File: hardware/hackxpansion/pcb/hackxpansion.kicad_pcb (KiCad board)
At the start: 4 copper layers, 52 x 65 mm, 101 parts, among them CN1 533981471, CN2 533981471, CN3 533981471, CN4 533981471, IC1 ADS7128IRTET, J1 Conn_01x03_MountingPin, J2 USB_C_Receptacle_USB2.0_14P, Q1 BSS138, Q2 2N7002, SW1 SW_Push, SW2 SW_Push, SW3 SW_On_Off, U2 RP2354B, U5 SPX3819M5-L-3-3, U7 BQ24075RGT, U8 USBLC6-2SC6, Y1 ABM8-272-T3

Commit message: updated part numbers
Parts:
- R22: value 3k9 -> 3k3
- R26, R27, R28, R29: value 5R -> 5R1

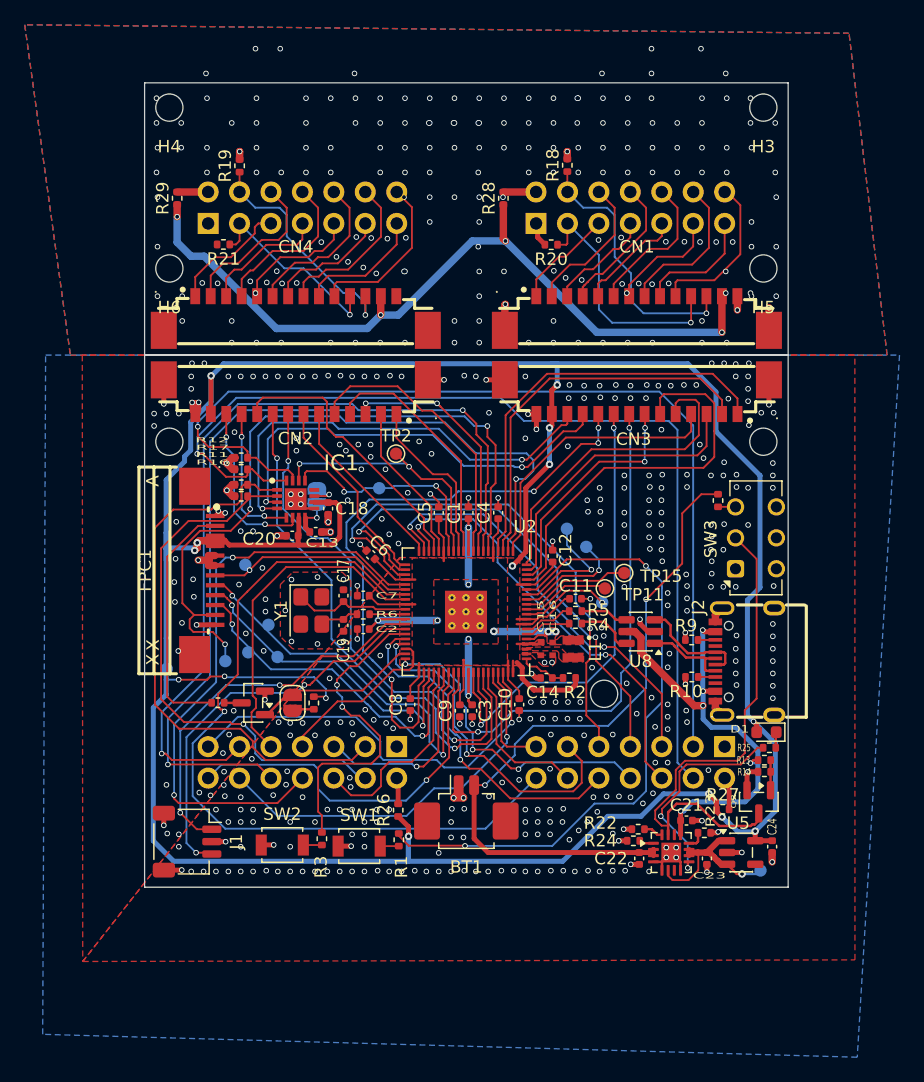
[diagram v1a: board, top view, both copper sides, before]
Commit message: added a bunch of gnd return VIAs, removed via group
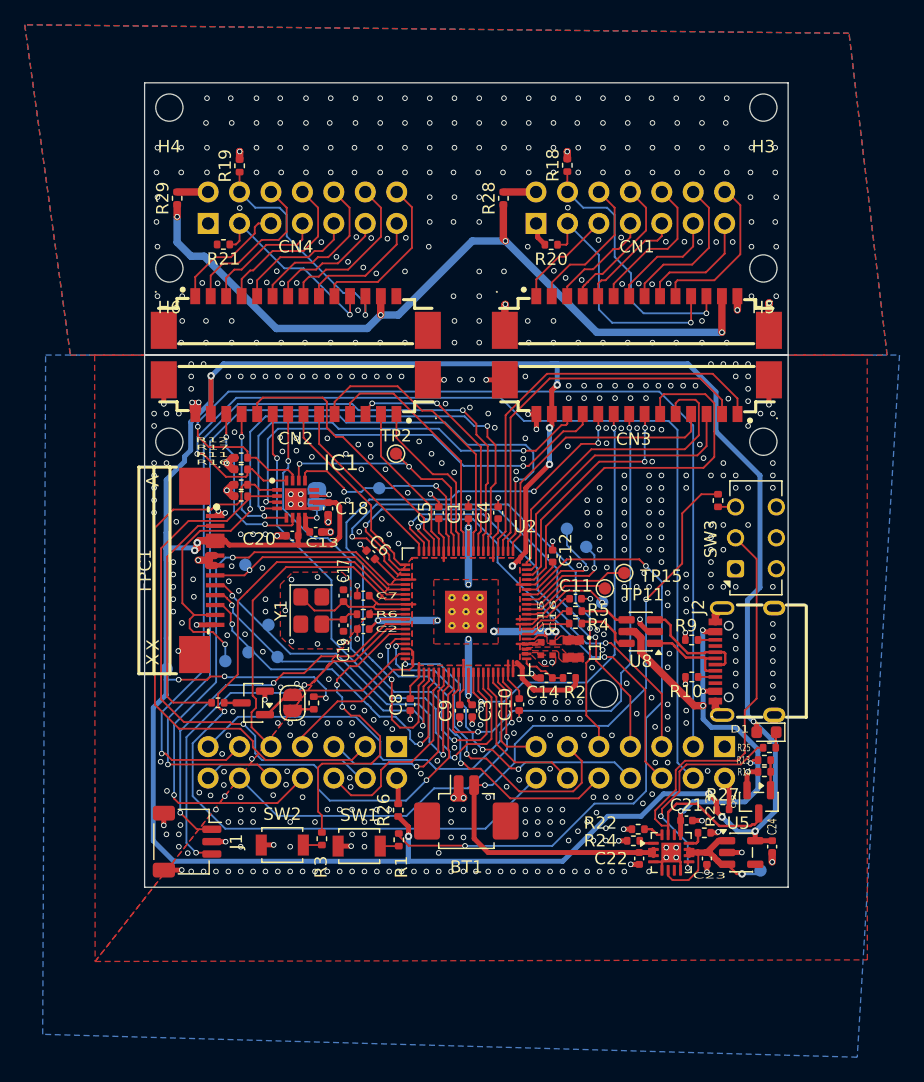
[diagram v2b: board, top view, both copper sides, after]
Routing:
- net /Connector Main Mod2/bank.GPIO8: track 37.2 -> 34.5 mm
- net /Connector Main Mod3/bank.GPIO8: track 43.8 -> 45.0 mm
- net /Main Board/Display/MOSI: track 27.6 -> 28.7 mm
- net /Main Board/Module Bay 1/GPIO2: track 41.1 -> 40.3 mm
- net Net-(U2-QSPI_SD1): track 10.2 -> 9.51 mm
- net /Connector Main Mod2/mod.MD1: track 35.9 -> 35.3 mm
- net Net-(U2-QSPI_SD2): track 9.15 -> 8.64 mm
- net /Main Board/Module Bay 0/GPIO8: track 33.8 -> 34.3 mm
- net /DAUGHT_GND: track 8.33 -> 8.75 mm, vias 177 -> 187
- net Net-(U4-3V3): vias 1 -> 0
- net /GND: vias 382 -> 439
- net /DAUGHT_+3V3: vias 6 -> 4
- net /Connector Daughter Mod3/bank.GPIO9: vias 1 -> 0
- net /Connector Daughter Mod3/bank.GPIO4: vias 1 -> 0
- net /Connector Daughter Mod2/bank.GPIO9: vias 1 -> 0
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
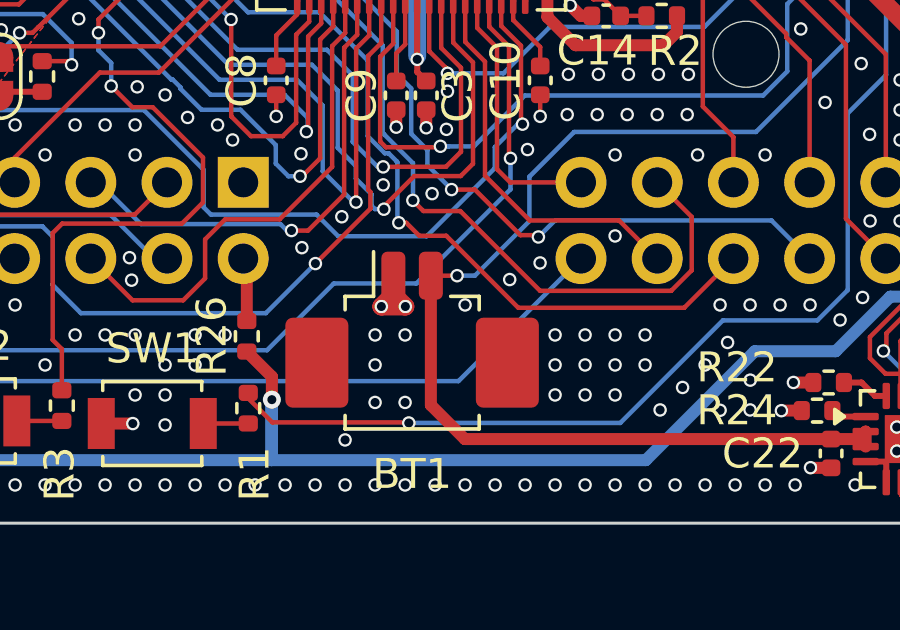
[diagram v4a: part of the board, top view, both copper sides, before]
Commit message: switched battery connectory polarity
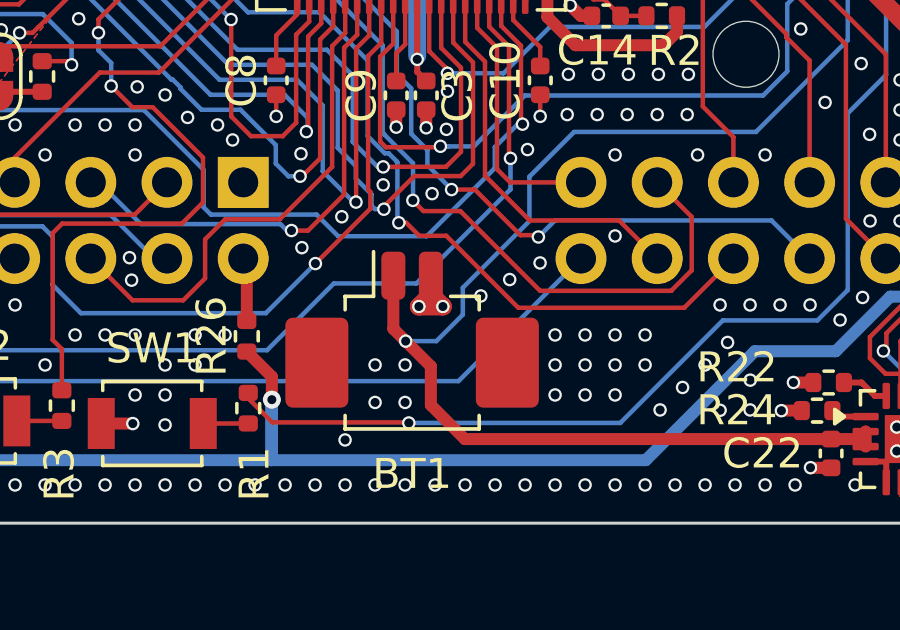
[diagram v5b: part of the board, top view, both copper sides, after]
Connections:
- BT1 pad 1: /GND -> /Main Board/Power/+BATT
- BT1 pad 2: /Main Board/Power/+BATT -> /GND
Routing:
- net /Main Board/Power/+BATT: track 56.8 -> 59.6 mm
- net /GND: vias 439 -> 438
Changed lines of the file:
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@@
 			(unit
 				(name "A")
-				(pins "2" "1")
+				(pins "1" "2")
 			)
 		)
@@
 			(layers "F.Cu" "F.Mask" "F.Paste")
 			(roundrect_rratio 0.25)
-			(net "/GND")
-			(pinfunction "-_1")
+			(net "/Main Board/Power/+BATT")
+			(pinfunction "+_1")
 			(pintype "passive")
 		)
@@
 			(layers "F.Cu" "F.Mask" "F.Paste")
 			(roundrect_rratio 0.25)
-			(net "/Main Board/Power/+BATT")
-			(pinfunction "+_2")
+			(net "/GND")
+			(pinfunction "-_2")
 			(pintype "passive")
 		)
@@
 	)
 	(segment
-		(start 126.844998 93.677787)
-		(end 127.244998 93.277787)
+		(start 128.094998 93.677787)
+		(end 128.494998 93.277787)
 		(width 0.6)
 		(layer "F.Cu")
@@
 	)
 	(segment
-		(start 127.644998 93.677787)
-		(end 126.844998 93.677787)
+		(start 128.894998 93.677787)
+		(end 128.094998 93.677787)
 		(width 0.6)
 		(layer "F.Cu")
@@
 	)
 	(segment
-		(start 127.644998 93.677787)
-		(end 127.244998 93.277787)
+		(start 128.894998 93.677787)
+		(end 128.494998 93.277787)
 		(width 0.6)
 		(layer "F.Cu")
@@
 	)
 	(segment
-		(start 127.244998 93.277787)
-		(end 127.244998 92.65)
+		(start 128.494998 93.277787)
+		(end 128.494998 92.65)
 		(width 0.6)
 		(layer "F.Cu")
@@
 	)
 	(via
-		(at 126.636 94.626)
-		(size 0.45)
-		(drill 0.3)
-		(layers "F.Cu" "B.Cu")
-		(net "/GND")
-	)
-	(via
 		(at 139.141587 96.131587)
 		(size 0.45)
@@
 	)
 	(via
+		(at 127.636 95.626)
+		(size 0.45)
+		(drill 0.3)
+		(layers "F.Cu" "B.Cu")
+		(free yes)
+		(net "/GND")
+	)
+	(via
 		(at 137.04 87.28)
 		(size 0.45)
@@
 	)
 	(via
-		(at 127.644998 93.677787)
+		(at 128.894998 93.677787)
 		(size 0.45)
 		(drill 0.3)
@@
 	)
 	(via
-		(at 129.636 93.626)
+		(at 130.161 93.326)
 		(size 0.45)
 		(drill 0.3)
@@
 	)
 	(via
-		(at 127.636 94.626)
-		(size 0.45)
-		(drill 0.3)
-		(layers "F.Cu" "B.Cu")
-		(net "/GND")
-	)
-	(via
 		(at 118.636 88.626)
 		(size 0.45)
@@
 	)
 	(via
-		(at 126.844998 93.677787)
+		(at 128.094998 93.677787)
 		(size 0.45)
 		(drill 0.3)
@@
 	)
 	(segment
-		(start 128.494998 92.65)
-		(end 128.494998 96.964998)
-		(width 0.4)
+		(start 145.31 74.74)
+		(end 145.31 70.69)
+		(width 0.15)
 		(layer "F.Cu")
 		(net "/Main Board/Power/+BATT")
 	)
 	(segment
-		(start 145.31 74.74)
-		(end 145.31 70.69)
-		(width 0.15)
+		(start 127.244998 92.65)
+		(end 127.244998 94.421825)
+		(width 0.4)
 		(layer "F.Cu")
 		(net "/Main Board/Power/+BATT")
@@
 	)
 	(segment
+		(start 127.244998 94.421825)
+		(end 127.655087 94.831913)
+		(width 0.4)
+		(layer "F.Cu")
+		(net "/Main Board/Power/+BATT")
+	)
+	(segment
 		(start 146.857421 69.142579)
 		(end 148.204862 69.142579)
@@
 	)
 	(segment
-		(start 129.37 92.65)
-		(end 128.494998 92.65)
-		(width 0.15)
+		(start 128.494998 95.671825)
+		(end 128.494998 96.964998)
+		(width 0.4)
 		(layer "F.Cu")
 		(net "/Main Board/Power/+BATT")
@@
 	)
 	(segment
+		(start 127.655087 94.831913)
+		(end 128.494998 95.671825)
+		(width 0.4)
+		(layer "F.Cu")
+		(net "/Main Board/Power/+BATT")
+	)
+	(segment
 		(start 142.41 77.64)
 		(end 145.31 74.74)
@@
 	)
 	(via
-		(at 129.37 92.65)
+		(at 142.39 77.64)
 		(size 0.45)
 		(drill 0.3)
@@
 	)
 	(via
-		(at 142.39 77.64)
+		(at 127.655087 94.831913)
 		(size 0.45)
 		(drill 0.3)
@@
 	)
 	(segment
-		(start 142.39 84.8)
-		(end 139.33 87.86)
+		(start 131.78 90.832)
+		(end 129.561 93.051)
+		(width 0.15)
+		(layer "B.Cu")
+		(net "/Main Board/Power/+BATT")
+	)
+	(segment
+		(start 142.39 77.64)
+		(end 142.39 84.8)
+		(width 0.15)
+		(layer "B.Cu")
+		(net "/Main Board/Power/+BATT")
+	)
+	(segment
+		(start 128.680087 94.831913)
+		(end 127.655087 94.831913)
 		(width 0.15)
 		(layer "B.Cu")
@@
 	)
 	(segment
-		(start 129.962 92.65)
-		(end 129.37 92.65)
+		(start 129.561 93.051)
+		(end 129.561 93.951)
 		(width 0.15)
 		(layer "B.Cu")
@@
 	)
 	(segment
-		(start 133.27 87.86)
-		(end 131.78 89.35)
+		(start 142.39 84.8)
+		(end 139.33 87.86)
 		(width 0.15)
 		(layer "B.Cu")
@@
 	)
 	(segment
-		(start 142.39 77.64)
-		(end 142.39 84.8)
+		(start 129.561 93.951)
+		(end 128.680087 94.831913)
 		(width 0.15)
 		(layer "B.Cu")
@@
 	)
 	(segment
-		(start 131.78 90.832)
-		(end 129.962 92.65)
+		(start 133.27 87.86)
+		(end 131.78 89.35)
 		(width 0.15)
 		(layer "B.Cu")
